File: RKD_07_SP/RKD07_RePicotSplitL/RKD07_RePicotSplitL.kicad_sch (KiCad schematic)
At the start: 18 parts, among them J1 Conn_01x24, J2 Conn_01x06, J3 Conn_01x06, J51 Conn_01x06, J52 Qwiic_RA, J53 RJ9, SW25 RotaryEncoder_Switch, SW31 SW_Push, SW53 SW_Push, SW55 SW_Push, U1 Pico

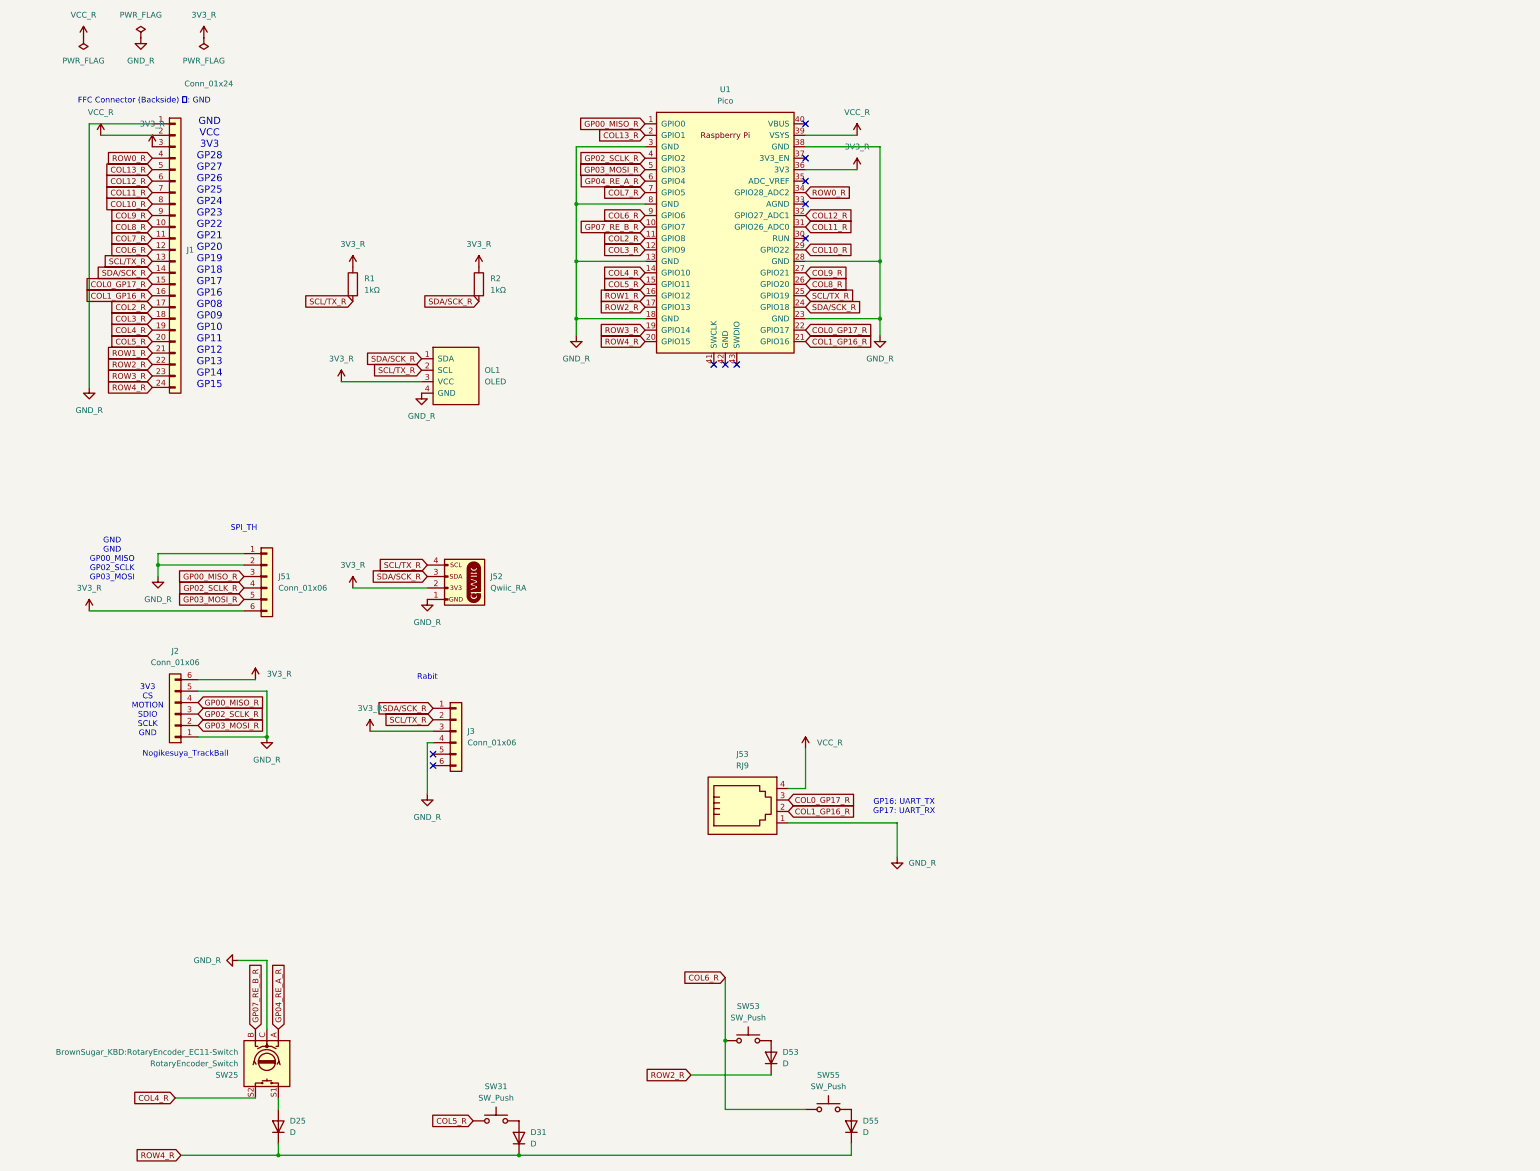
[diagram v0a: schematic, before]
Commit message: Add SplitL
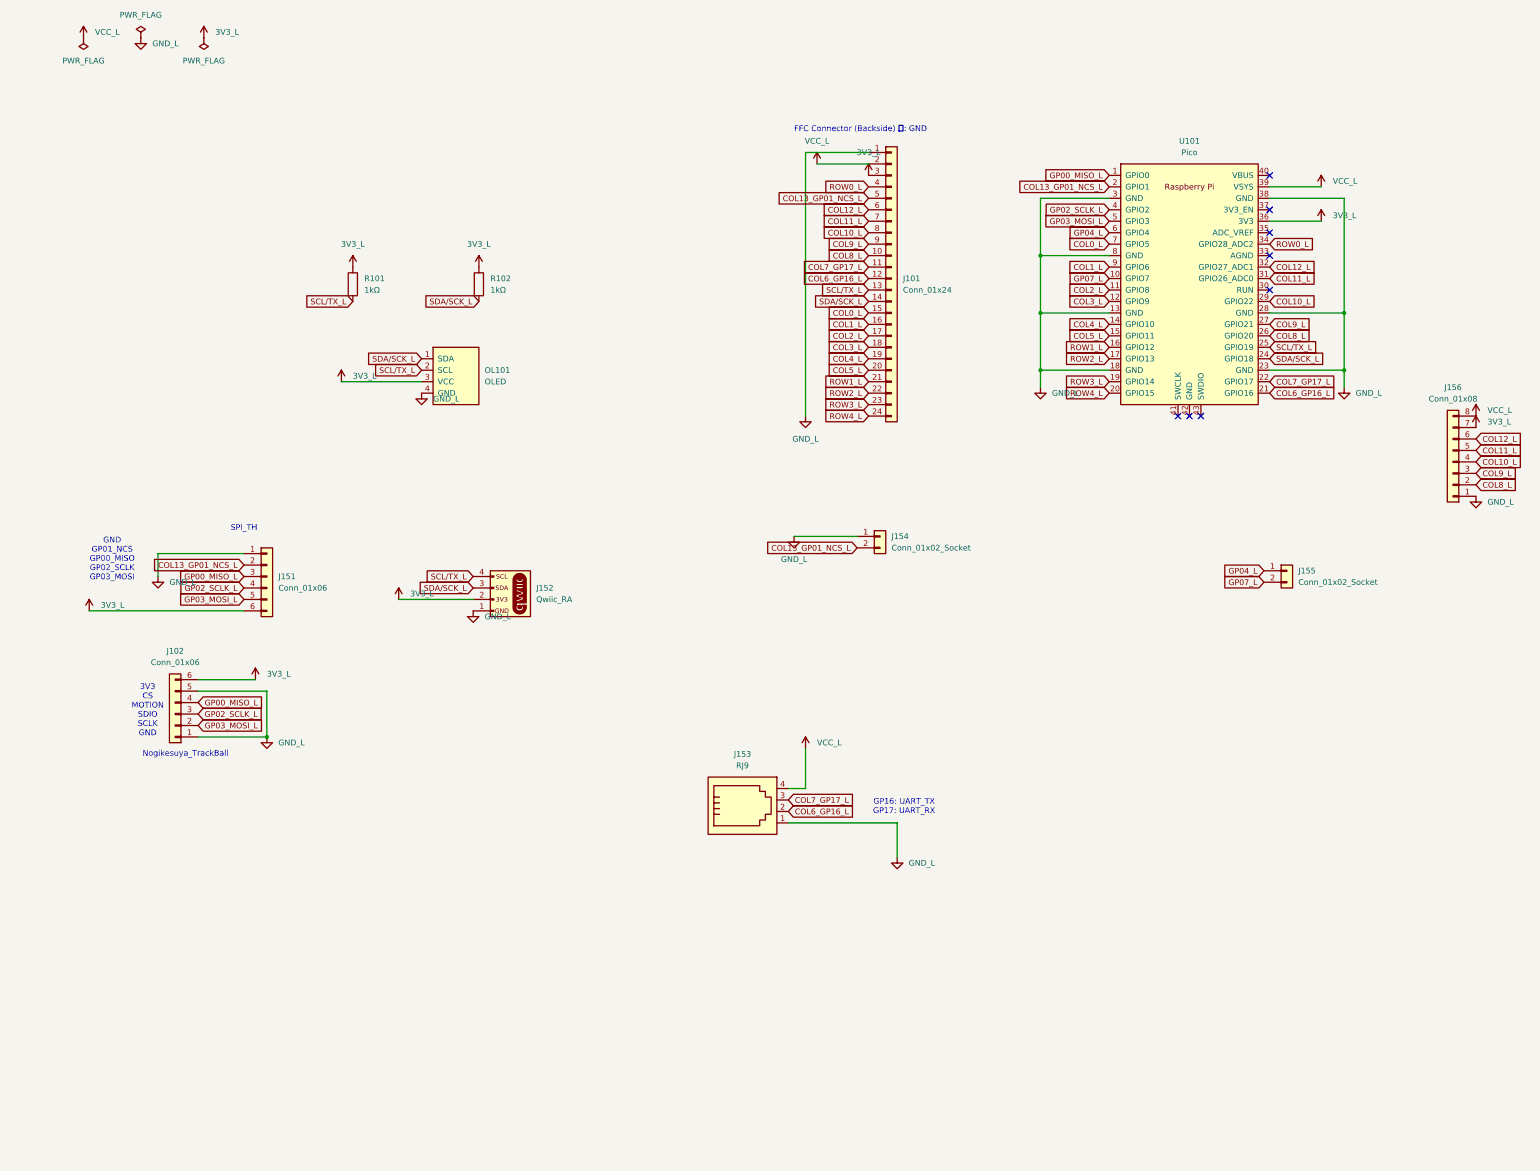
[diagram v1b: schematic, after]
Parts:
- removed D25, D31, D53, D55: D, kbd_Parts:Diode_SMD, symbol Device:D
- removed J1: Conn_01x24, Connector_FFC-FPC:Hirose_FH12-24S-0.5SH_1x24-1MP_P0.50mm_Horizontal, symbol Connector_Generic:Conn_01x24
- removed J3: Conn_01x06, DreaM117er-keebLibrary:Hirose_FH12-6S-0.5SH_1x06-1MP_P0.50mm_Horizontal, symbol Connector_Generic:Conn_01x06
- removed SW25: RotaryEncoder_Switch, BrownSugar_KBD:RotaryEncoder_EC11-Switch, symbol Device:RotaryEncoder_Switch
- removed SW31, SW53, SW55: SW_Push, Rikkodo_FootPrint:rkd_Asm_ChocV1V2_Hotswap_1u, symbol Switch:SW_Push
- added J101: Conn_01x24, Connector_FFC-FPC:Hirose_FH12-24S-0.5SH_1x24-1MP_P0.50mm_Horizontal, symbol Connector_Generic:Conn_01x24
- added J154, J155: Conn_01x02_Socket, Connector_PinHeader_2.54mm:PinHeader_1x02_P2.54mm_Vertical, symbol Connector_Generic:Conn_01x02
- added J156: Conn_01x08, Connector_PinHeader_2.54mm:PinHeader_1x08_P2.54mm_Vertical, symbol Connector_Generic:Conn_01x08
- J151: renamed from J51; footprint Connector_PinHeader_2.54mm:PinHeader_1x06_P2.54mm_Horizontal -> Connector_PinHeader_2.54mm:PinHeader_1x06_P2.54mm_Vertical
- renumbered J2 to J102, J52 to J152, J53 to J153, OL1 to OL101, R1 to R101, R2 to R102, U1 to U101
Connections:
- net 3V3_R renamed 3V3_L
- net 3V3_L: now also J101.3 (Pin_3), J156.7 (Pin_7)
- net COL0_GP17_R renamed COL7_GP17_L
- net COL7_GP17_L: now also J101.11 (Pin_11)
- net COL10_R renamed COL10_L
- net COL10_L: now also J101.8 (Pin_8), J156.4 (Pin_4)
- net COL11_R renamed COL11_L
- net COL11_L: now also J101.7 (Pin_7), J156.5 (Pin_5)
- net COL12_R renamed COL12_L
- net COL12_L: now also J101.6 (Pin_6), J156.6 (Pin_6)
- net COL13_R renamed COL13_GP01_NCS_L
- net COL13_GP01_NCS_L: now also J151.2 (Pin_2), J101.5 (Pin_5), J154.2 (Pin_2)
- net COL1_GP16_R renamed COL6_GP16_L
- net COL6_GP16_L: now also J101.12 (Pin_12)
- net COL2_R renamed COL2_L
- net COL2_L: now also J101.17 (Pin_17)
- net COL3_R renamed COL3_L
- net COL3_L: now also J101.18 (Pin_18)
- net COL4_R renamed COL4_L
- net COL4_L: now also J101.19 (Pin_19)
- net COL5_R renamed COL5_L
- net COL5_L: now also J101.20 (Pin_20)
- net COL6_R renamed COL1_L
- net COL1_L: now also J101.16 (Pin_16)
- net COL7_R renamed COL0_L
- net COL0_L: now also J101.15 (Pin_15)
- net COL8_R renamed COL8_L
- net COL8_L: now also J101.10 (Pin_10), J156.2 (Pin_2)
- net COL9_R renamed COL9_L
- net COL9_L: now also J101.9 (Pin_9), J156.3 (Pin_3)
- net GND_R renamed GND_L
- net GND_L: now also J101.1 (Pin_1), J154.1 (Pin_1), J156.1 (Pin_1); no longer J151.2 (Pin_2)
- net GP00_MISO_R renamed GP00_MISO_L
- net GP02_SCLK_R renamed GP02_SCLK_L
- net GP03_MOSI_R renamed GP03_MOSI_L
- net GP04_RE_A_R renamed GP04_L
- net GP04_L: now also J155.1 (Pin_1)
- net GP07_RE_B_R renamed GP07_L
- net GP07_L: now also J155.2 (Pin_2)
- net ROW0_R renamed ROW0_L
- net ROW0_L: now also J101.4 (Pin_4)
- net ROW1_R renamed ROW1_L
- net ROW1_L: now also J101.21 (Pin_21)
- net ROW2_R renamed ROW2_L
- net ROW2_L: now also J101.22 (Pin_22)
- net ROW3_R renamed ROW3_L
- net ROW3_L: now also J101.23 (Pin_23)
- net ROW4_R renamed ROW4_L
- net ROW4_L: now also J101.24 (Pin_24)
- net SCL/TX_R renamed SCL/TX_L
- net SCL/TX_L: now also J101.13 (Pin_13)
- net SDA/SCK_R renamed SDA/SCK_L
- net SDA/SCK_L: now also J101.14 (Pin_14)
- net VCC_R renamed VCC_L
- net VCC_L: now also J101.2 (Pin_2), J156.8 (Pin_8)
- no-connect marks 10 -> 8
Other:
- note added: "GND GP01_NCS GP00_MISO GP02_SCLK GP03_MOSI"
- note removed: "GND GND GP00_MISO GP02_SCLK GP03_MOSI"
- note removed: "GND VCC 3V3 GP28 GP27 GP26 GP25 GP24 GP23 GP22 GP21 GP20 GP19 GP18 GP17 GP16 GP08 GP09 GP10 GP11 GP12 GP13 GP14 GP15"
- note removed: "Rabit"
- moved on the sheet: J152, U101

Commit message: RePicotUpdate
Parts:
- removed J154: Conn_01x02_Socket, Connector_PinHeader_2.54mm:PinHeader_1x02_P2.54mm_Vertical, symbol Connector_Generic:Conn_01x02
- added J１03: Conn_01x06, DreaM117er-keebLibrary:Hirose_FH12-6S-0.5SH_1x06-1MP_P0.50mm_Horizontal, symbol Connector_Generic:Conn_01x06
- J151: footprint Connector_PinHeader_2.54mm:PinHeader_1x06_P2.54mm_Vertical -> Connector_PinHeader_2.54mm:PinHeader_1x08_P2.54mm_Vertical; symbol Connector_Generic:Conn_01x06 -> Connector_Generic:Conn_01x08
- renumbered J155 to J154, J156 to J155
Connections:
- net 3V3_L: now also J151.8 (Pin_8), J１03.3 (Pin_3); no longer J151.6 (Pin_6)
- net COL13_GP01_NCS_L: now also J151.4 (Pin_4); no longer J151.2 (Pin_2)
- net GND_L: now also J151.2 (Pin_2), J151.3 (Pin_3), J１03.4 (Pin_4)
- net GP00_MISO_L: now also J151.5 (Pin_5); no longer J151.3 (Pin_3)
- net GP02_SCLK_L: now also J151.6 (Pin_6); no longer J151.4 (Pin_4)
- net GP03_MOSI_L: now also J151.7 (Pin_7); no longer J151.5 (Pin_5)
- net SCL/TX_L: now also J１03.2 (Pin_2)
- net SDA/SCK_L: now also J１03.1 (Pin_1)
- no-connect marks 8 -> 10
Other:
- note added: "Rabit"

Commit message: update
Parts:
- removed J153: RJ9, Connector_RJ:RJ9_Evercom_5301-440xxx_Horizontal, symbol Connector:RJ9
- added J153: 6P6C, Connector_RJ:RJ12_Amphenol_54601-x06_Horizontal, symbol Connector:6P6C
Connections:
- net COL6_GP16_L: now also J153.3
- net COL7_GP17_L: now also J153.4
- net GND_L: now also J153.2
- net VCC_L: now also J153.5
- no-connect marks 10 -> 12
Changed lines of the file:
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@@
 	)
 	(no_connect
+		(at 173.99 199.39)
+	)
+	(no_connect
 		(at 90.17 176.53)
 	)
@@
 	)
 	(no_connect
+		(at 173.99 186.69)
+	)
+	(no_connect
 		(at 280.67 71.12)
 	)
@@
 	)
 	(symbol
-		(lib_id "Connector:RJ9")
-		(at 163.83 194.31 0)
-		(unit 1)
-		(exclude_from_sim no)
-		(in_bom yes)
-		(on_board yes)
-		(dnp no)
-		(fields_autoplaced yes)
-		(property "Reference" "J153"
-			(at 163.83 181.61 0)
-			(effects
-				(font
-					(size 1.27 1.27)
-				)
-			)
-		)
-		(property "Value" "RJ9"
-			(at 163.83 184.15 0)
-			(effects
-				(font
-					(size 1.27 1.27)
-				)
-			)
-		)
-		(property "Footprint" "Connector_RJ:RJ9_Evercom_5301-440xxx_Horizontal"
-			(at 163.83 193.04 90)
-			(effects
-				(font
-					(size 1.27 1.27)
-				)
-				(hide yes)
-			)
-		)
-		(property "Datasheet" "~"
-			(at 163.83 193.04 90)
-			(effects
-				(font
-					(size 1.27 1.27)
-				)
-				(hide yes)
-			)
-		)
-		(property "Description" "RJ connector, 4P4C (4 positions 4 connected)"
-			(at 163.83 194.31 0)
-			(effects
-				(font
-					(size 1.27 1.27)
-				)
-				(hide yes)
-			)
-		)
-		(pin "4"
-		)
-		(pin "1"
-		)
-		(pin "3"
-		)
-		(pin "2"
-		)
-		(instances
-			(project "RKD07_RePicotSplitR"
-				(path "/237aa5e6-259c-459d-b408-55413a51412a"
-					(reference "J153")
-					(unit 1)
-				)
-			)
-		)
-	)
-	(symbol
 		(lib_id "Device:R")
 		(at 105.41 77.47 0)
@@
 					(unit 1)
 				)
+			)
+		)
+	)
+	(symbol
+		(lib_id "Connector:6P6C")
+		(at 163.83 194.31 0)
+		(unit 1)
+		(exclude_from_sim no)
+		(in_bom yes)
+		(on_board yes)
+		(dnp no)
+		(fields_autoplaced yes)
+		(property "Reference" "J153"
+			(at 163.83 179.07 0)
+			(effects
+				(font
+					(size 1.27 1.27)
+				)
+			)
+		)
+		(property "Value" "6P6C"
+			(at 163.83 181.61 0)
+			(effects
+				(font
+					(size 1.27 1.27)
+				)
+			)
+		)
+		(property "Footprint" "Connector_RJ:RJ12_Amphenol_54601-x06_Horizontal"
+			(at 163.83 193.675 90)
+			(effects
+				(font
+					(size 1.27 1.27)
+				)
+				(hide yes)
+			)
+		)
+		(property "Datasheet" "~"
+			(at 163.83 193.675 90)
+			(effects
+				(font
+					(size 1.27 1.27)
+				)
+				(hide yes)
+			)
+		)
+		(property "Description" "RJ connector, 6P6C (6 positions 6 connected), RJ12/RJ18/RJ25"
+			(at 163.83 194.31 0)
+			(effects
+				(font
+					(size 1.27 1.27)
+				)
+				(hide yes)
+			)
+		)
+		(pin "4"
+		)
+		(pin "1"
+		)
+		(pin "5"
+		)
+		(pin "2"
+		)
+		(pin "3"
+		)
+		(pin "6"
+		)
+		(instances
+			(project "RKD07_RePicotSplitL"
+				(path "/237aa5e6-259c-459d-b408-55413a51412a"
+					(reference "J153")
+					(unit 1)
+				)
